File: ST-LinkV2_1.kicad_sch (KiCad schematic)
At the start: 32 parts, among them J201 TYPE-C-14PLC-H10.0, J202 Conn_01x01, J203 Conn_01x01, J204 Conn_01x01, J205 Conn_01x01, U201 STM32F103CBTx, Y201 NX3225GD-8MHZ-STD-CRA-3

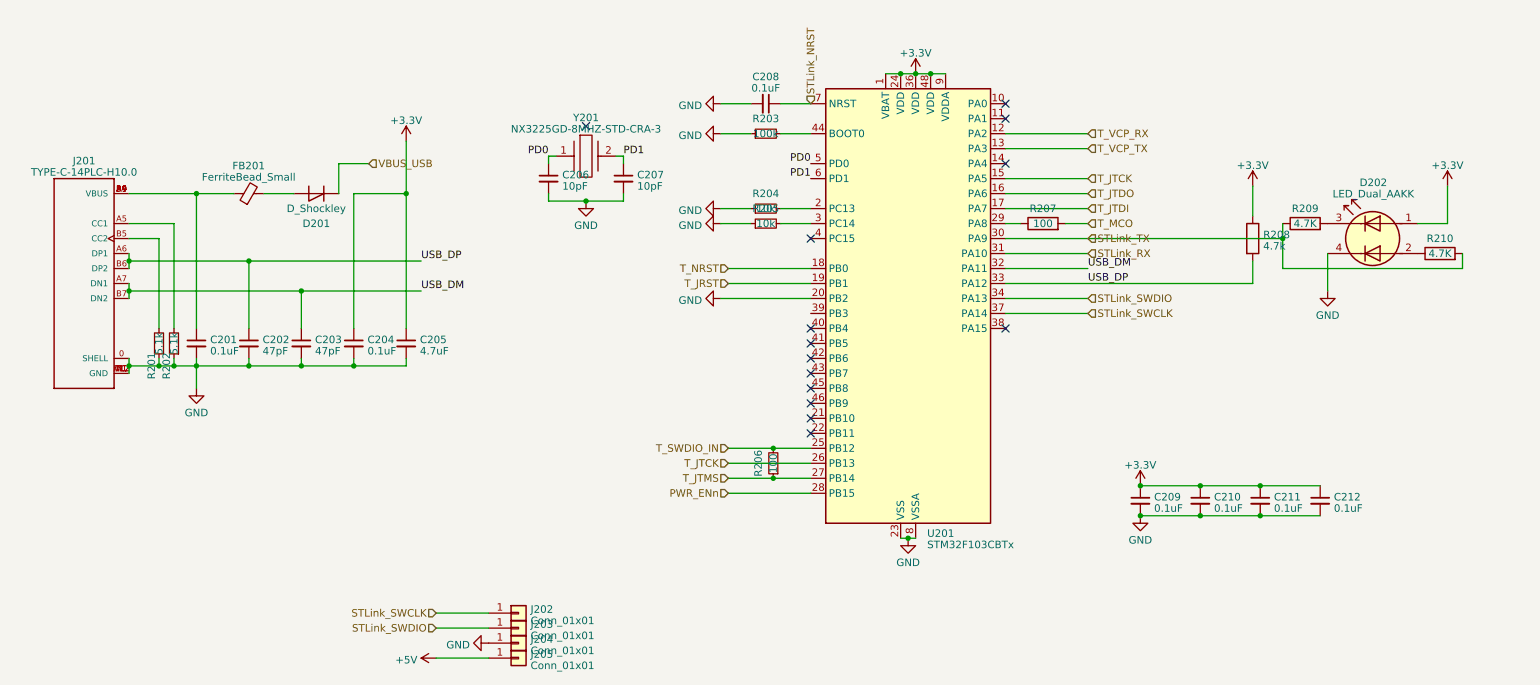
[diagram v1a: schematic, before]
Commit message: Fix ST-link reset
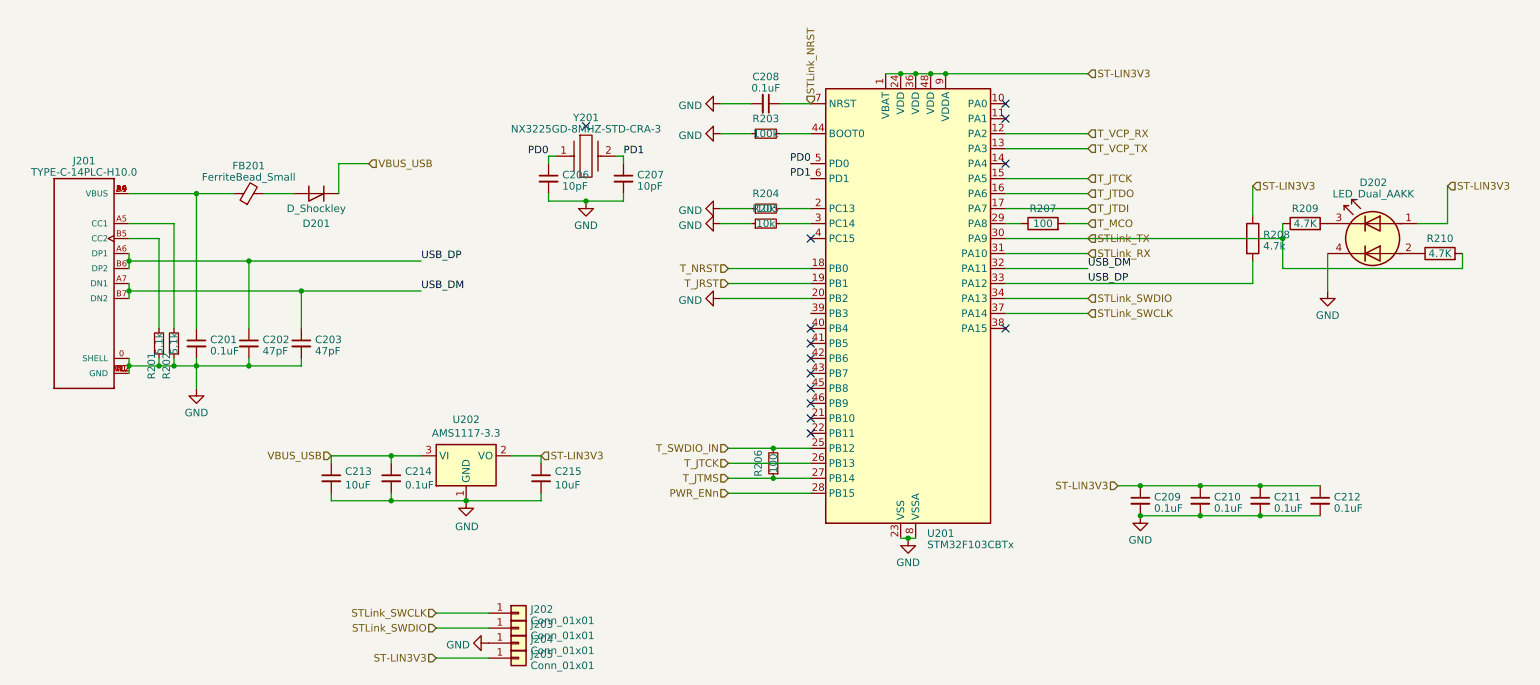
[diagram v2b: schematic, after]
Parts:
- removed C204: 0.1uF, Capacitor_SMD:C_0402_1005Metric, symbol Device:C_Small
- removed C205: 4.7uF, Capacitor_SMD:C_0805_2012Metric, symbol Device:C_Small
- added C213, C215: 10uF, Capacitor_SMD:C_0805_2012Metric, symbol Device:C_Small
- added C214: 0.1uF, Capacitor_SMD:C_0402_1005Metric, symbol Device:C_Small
- added U202: AMS1117-3.3, Package_TO_SOT_SMD:SOT-89-3, symbol Regulator_Linear:AMS1117-3.3
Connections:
- net +5V is gone; now on net ST-LIN3V3: J205.1 (Pin_1)
- net GND: now also C213.2, C214.2, C215.2, U202.1 (GND)
- net VBUS_USB: now also C213.1, C214.1, U202.3 (VI)
- net +3.3V renamed ST-LIN3V3
- net ST-LIN3V3: now also C215.1, U202.2 (VO)
